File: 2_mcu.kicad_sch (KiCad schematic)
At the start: 33 parts, among them J1 SWD TagConnect, J201 Conn_01x05_Pin, SW201 PTS815 SJK, U201 STM32F446RETx, Y201 16MHz

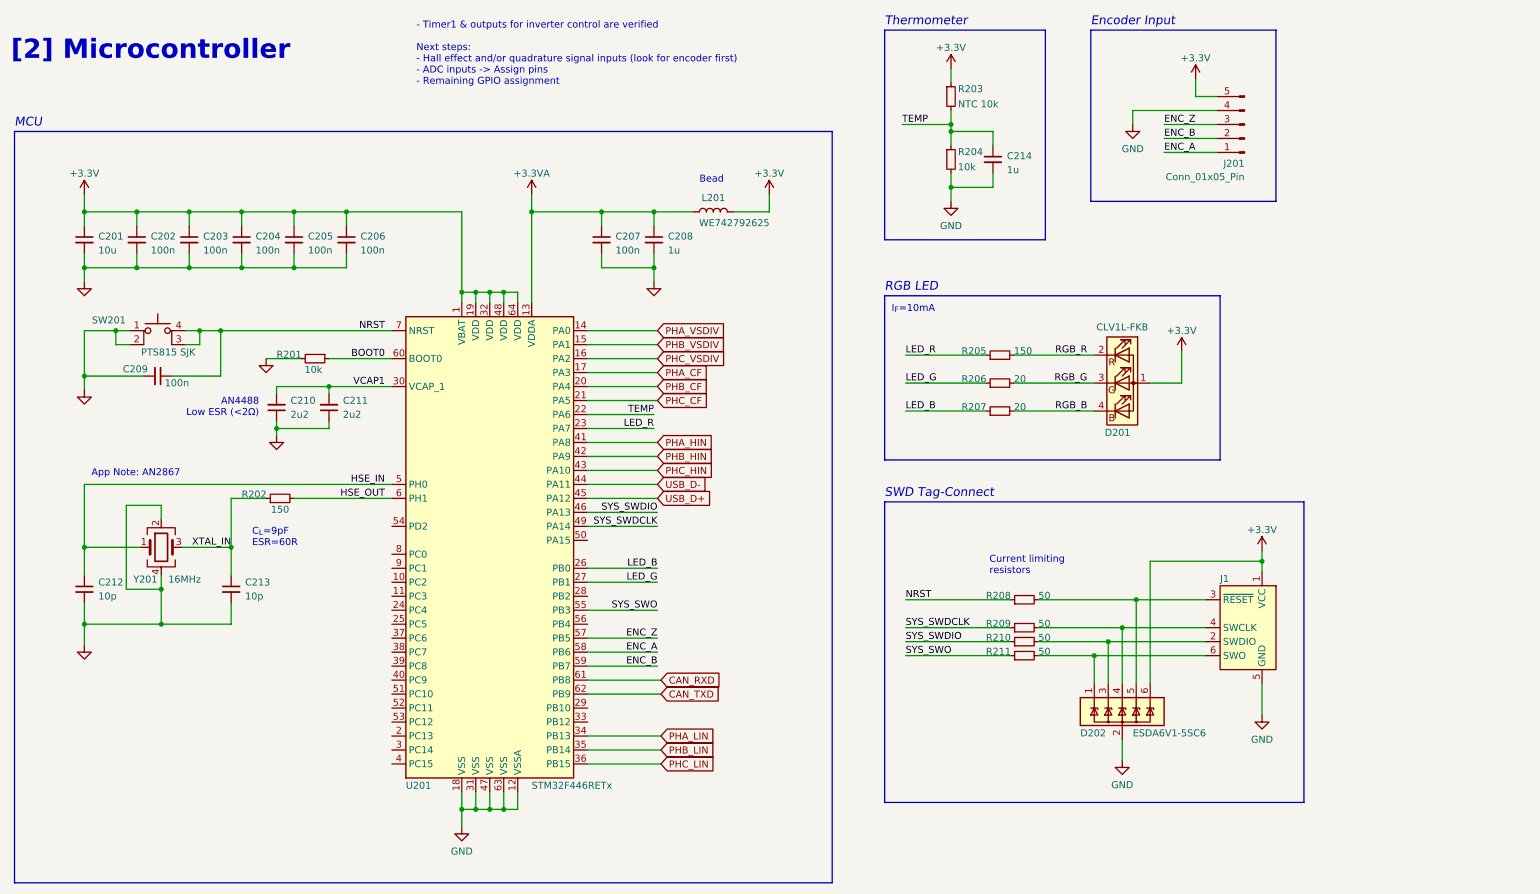
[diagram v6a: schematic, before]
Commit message: feat: footprint assignment, circuit check and routing kickoff
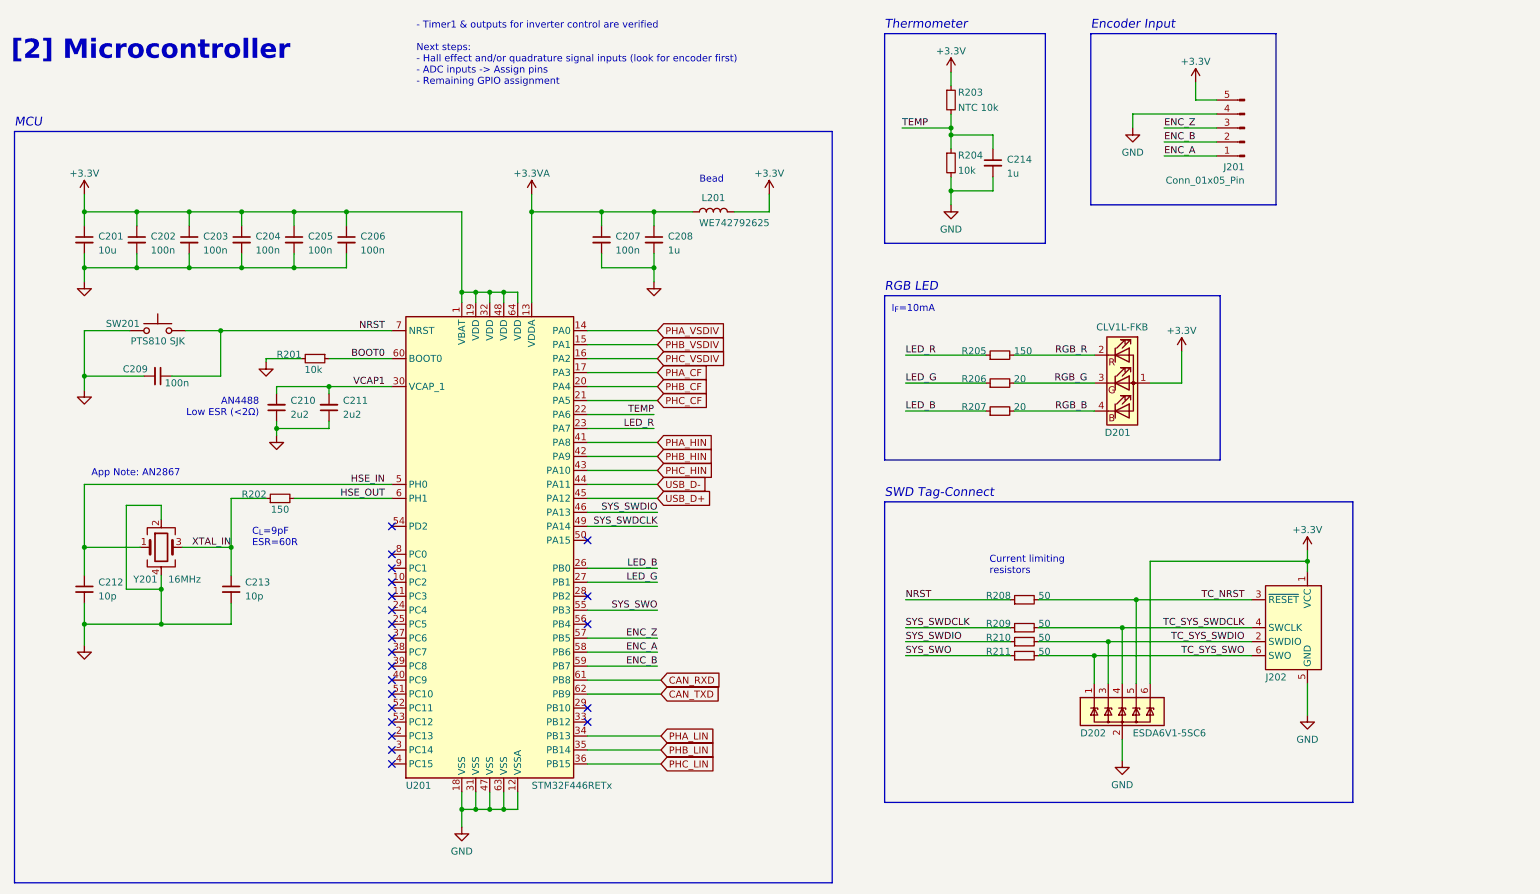
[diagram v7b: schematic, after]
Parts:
- removed SW201: PTS815 SJK, symbol Switch:SW_MEC_5E
- added SW201: PTS810 SJK, Button_Switch_SMD:SW_SPST_PTS810, symbol Switch:SW_Push
- C201, C208, C210, C211, C214: footprint (none) -> Capacitor_SMD:C_0603_1608Metric_Pad1.08x0.95mm_HandSolder
- C202, C203, C204, C205, C206, C207, C209: footprint (none) -> Capacitor_SMD:C_0402_1005Metric_Pad0.74x0.62mm_HandSolder
- J201: footprint (none) -> Connector_PinHeader_2.54mm:PinHeader_1x05_P2.54mm_Vertical
- L201: footprint (none) -> Inductor_SMD:L_0603_1608Metric_Pad1.05x0.95mm_HandSolder; Link (none) -> https://www.digikey.de/en/products/detail/w%C3%BCrth-elektr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
- renumbered J1 to J202
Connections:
- net GND: now also SW201.1
- net NRST: now also SW201.2
- net TC_SYS_SWO: now reaches D202.1 (IO1), J202.6 (SWO), R211.2
- net TC_SYS_SWDIO: now reaches D202.3 (IO2), J202.2 (SWDIO), R210.2
- net TC_SYS_SWDCLK: now reaches D202.4 (IO3), J202.4 (SWCLK), R209.2
- net TC_NRST: now reaches D202.5 (IO4), J202.3 (~{RESET}), R208.2
- no-connect marks 0 -> 22
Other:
- moved on the sheet: C214, J201, J202, R203, R204
